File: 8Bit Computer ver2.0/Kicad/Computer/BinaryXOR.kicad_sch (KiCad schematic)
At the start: 4 parts, among them IC101 SN74LVC1G14DBVR, IC103 SN74AHC74DR, IC104 SN74ABT574ADWR, IC98 SN74LVC1G86DBVR

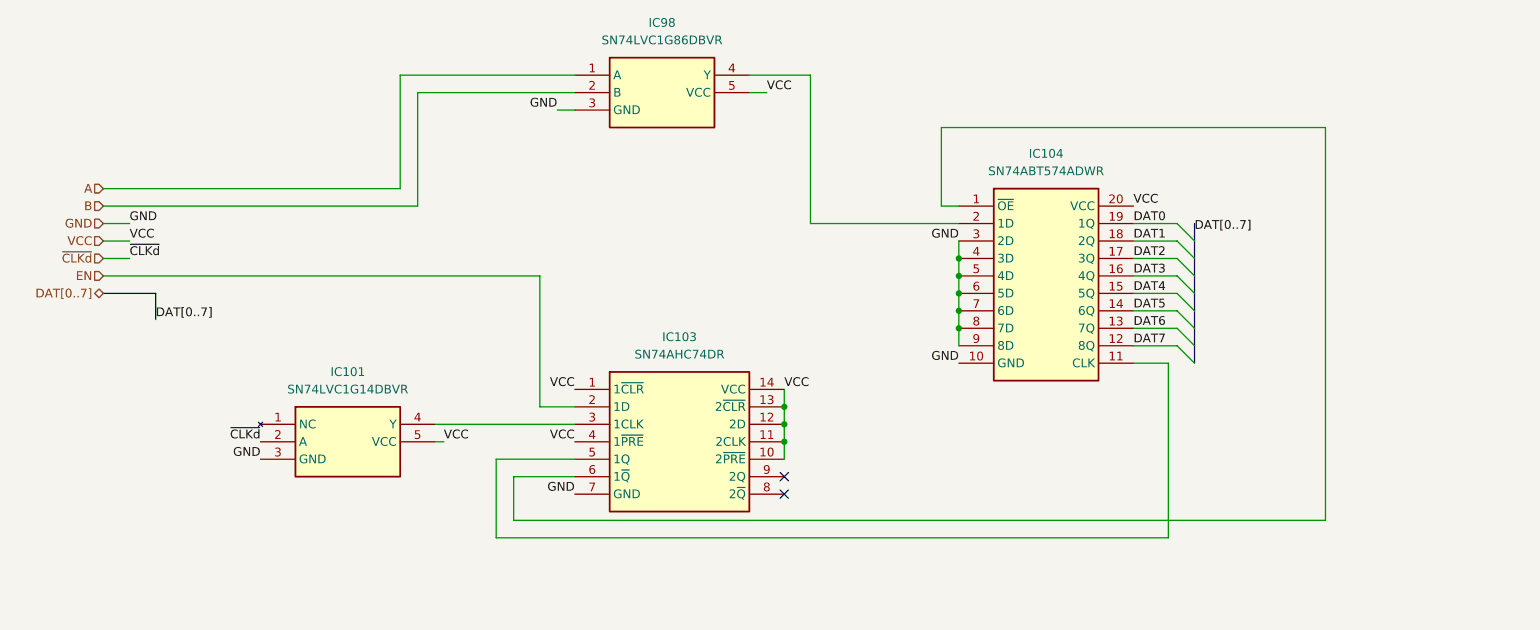
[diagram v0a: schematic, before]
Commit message: changed page numbers, compressed ROOT file from A1 to A4
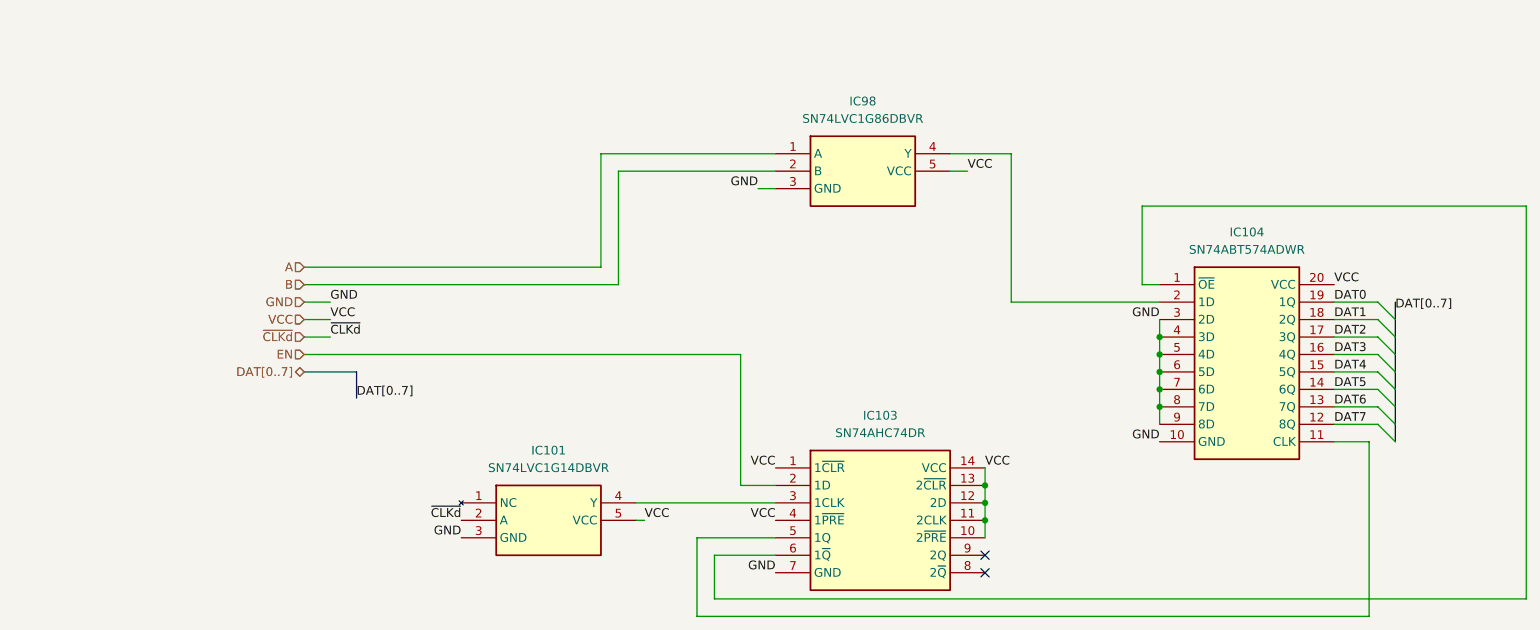
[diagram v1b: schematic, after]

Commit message: changed page numbers, every schematic is now A4
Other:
- title: (none) -> ${SHEETNAME}
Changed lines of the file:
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@@
 	(generator_version "9.0")
 	(paper "A4")
+	(title_block
+		(title "${SHEETNAME}")
+		(date "2026-03-21")
+		(rev "2.7")
+	)
 	(junction
 		(at 179.07 99.06)
